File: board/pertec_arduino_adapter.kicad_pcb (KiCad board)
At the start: 2 copper layers, 88.9 x 78.7 mm, 47 parts, among them J1 Conn_02x25_Odd_Even, J2 Conn_02x25_Odd_Even, J3 Conn_02x03_Odd_Even, J4 Conn_01x24, J5 Conn_01x24, J6 Conn_01x05, J7 RJ45_Cetus_J1B1211CCD, J8 Conn_02x03_Odd_Even, Q1 BSS138, Q2 BSS138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

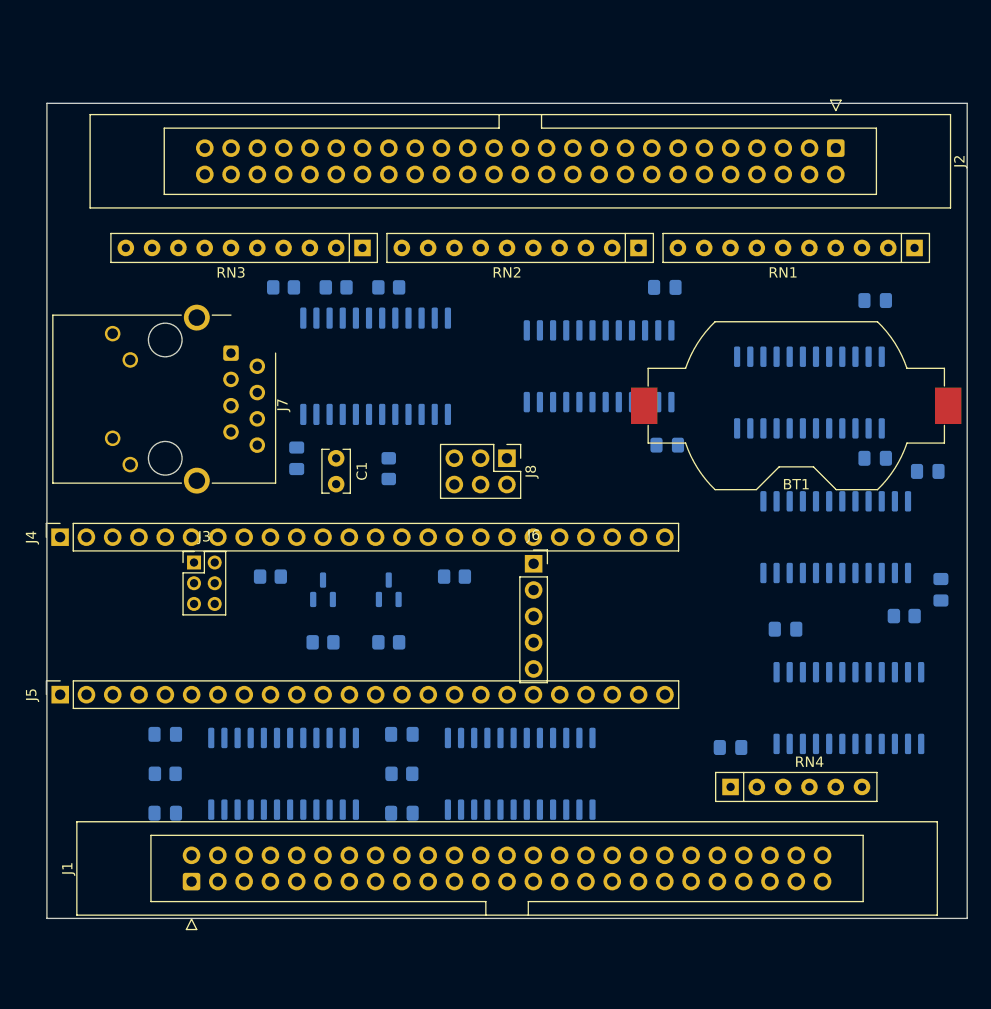
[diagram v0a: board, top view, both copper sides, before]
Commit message: Development checkpoint: added switchable controller/peripheral functionality.
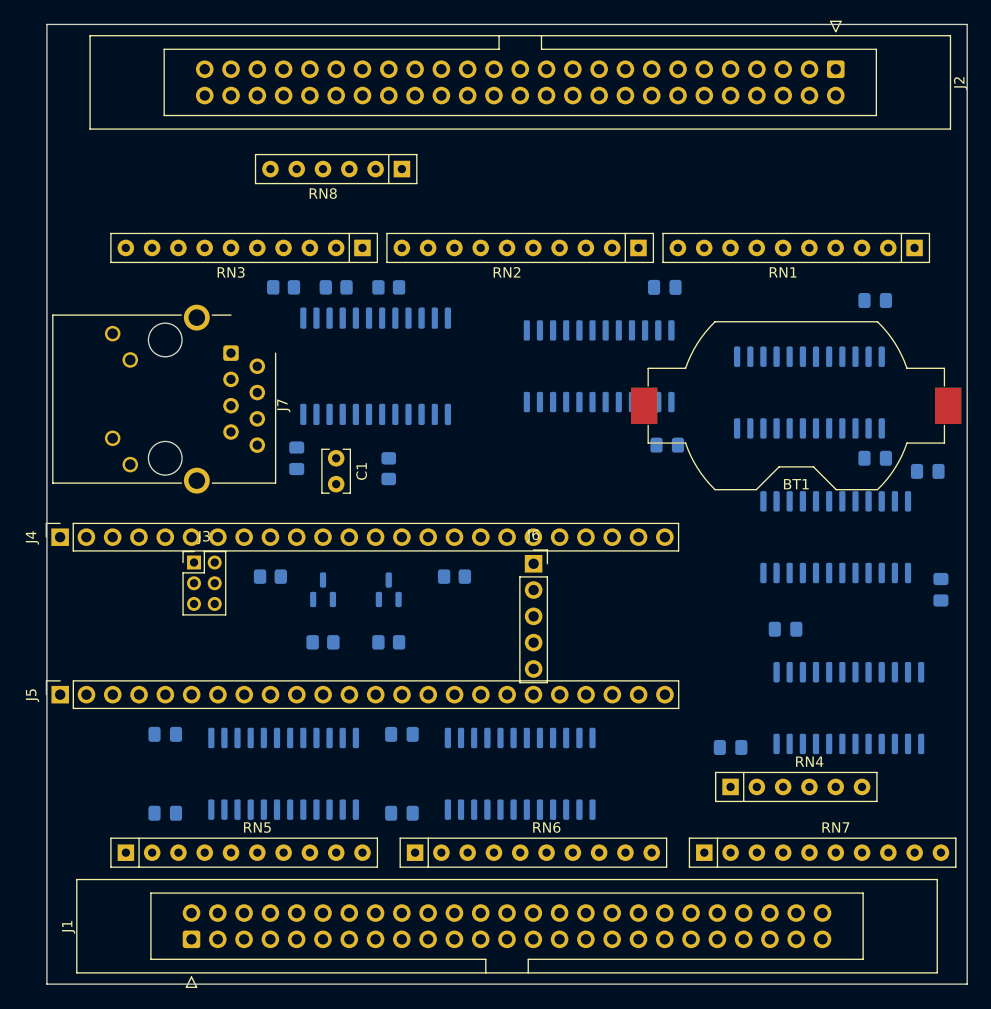
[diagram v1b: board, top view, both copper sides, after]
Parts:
- removed J8: Conn_02x03_Odd_Even, pertec_arduino_adapter:PinHeader_2x03_P2.54mm_Vertical
- removed R10, R11, R9: 10 kΩ, pertec_arduino_adapter:R_0805_2012Metric_Pad1.20x1.40mm_HandSolder
- added RN5: R1=220Ω, R2=330Ω, pertec_arduino_adapter:R_Array_SIP10, F.Cu at (94.0, 118.1)
- added RN6: R1=220Ω, R2=330Ω, pertec_arduino_adapter:R_Array_SIP10, F.Cu at (121.9, 118.1)
- added RN7: R1=220Ω, R2=330Ω, pertec_arduino_adapter:R_Array_SIP10, F.Cu at (149.9, 118.1)
- added RN8: R1=220Ω, R2=330Ω, pertec_arduino_adapter:R_Array_SIP6, F.Cu at (120.7, 52.1)
- moved J2 7.62 mm to (162.6, 42.4)
- moved J1 5.58 mm to (100.3, 126.5)
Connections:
- net GPIO_AD_B0_02 renamed LVIRP
- net GPIO_AD_B0_03 renamed LVIFMK
- net GPIO_AD_B0_12 renamed LPI2C4_SCL
- net GPIO_AD_B0_13 renamed LPI2C4_SDA
- net GPIO_AD_B1_00 renamed LVIR7
- net GPIO_AD_B1_01 renamed LVIR6
- net GPIO_AD_B1_02 renamed LVIR5
- net GPIO_AD_B1_03 renamed LVIR4
- net GPIO_AD_B1_04 renamed LVIR3
- net GPIO_AD_B1_05 renamed LVIR2
- net GPIO_AD_B1_06 renamed LVIR1
- net GPIO_AD_B1_07 renamed LVIR0
- net GPIO_AD_B1_08 renamed LVIW7
- net GPIO_AD_B1_09 renamed LVIW6
- net GPIO_AD_B1_10 renamed LVIW5
- net GPIO_AD_B1_11 renamed LVIW4
- net GPIO_AD_B1_12 renamed LVIW3
- net GPIO_AD_B1_13 renamed LVIW2
- net GPIO_AD_B1_14 renamed LVIW1
- net GPIO_AD_B1_15 renamed LVIW0
- net GPIO_B0_00 renamed LVIWRT
- net GPIO_B0_01 renamed LVIERASE
- net GPIO_B0_02 renamed LVIEDIT
- net GPIO_B0_03 renamed LVILWD
- net GPIO_B0_10 renamed LVIGO
- net GPIO_B0_11 renamed LVIREV
- net GPIO_B0_12 renamed LVIWFM
- net GPIO_B1_00 renamed LVIREW
- net GPIO_B1_01 renamed LVIWP
- net GPIO_B1_02 renamed LVIRSTR
- net GPIO_B1_03 renamed LVIWSTR
- net GPIO_B1_12 renamed LVIHER
- net GPIO_B1_13 renamed LVICER
- net GPIO_EMC_04 renamed LVIRDY
- net GPIO_EMC_06 renamed LVIDBY
- net GPIO_EMC_07 renamed LVIFBY
- net GPIO_EMC_08 renamed ~{LPI2C4_INT}
- net GPIO_EMC_36 renamed LVIEOT
- net GPIO_EMC_37 renamed LVIOFL
- J5 pad 20: GPIO_EMC_32 -> DIRB
- J5 pad 21: GPIO_EMC_31 -> OEA
- J5 pad 5: GPIO_EMC_05 -> DIRA
- U1 pad 18: ILDP -> unconnected-(U1-Pad18)
- U1 pad 2: GNDREF -> DIRA
- U1 pad 22: GNDREF -> OEA
- U1 pad 6: GPIO_EMC_32 -> unconnected-(U1-Pad6)
- U2 pad 2: Net-(U2-Pad2) -> DIRB
- U3 pad 17: IFPT -> unconnected-(U3-Pad17)
- U3 pad 2: GNDREF -> DIRA
- U3 pad 22: GNDREF -> OEA
- U3 pad 7: GPIO_EMC_05 -> unconnected-(U3-Pad7)
- U4 pad 2: Net-(U4-Pad2) -> DIRB
- U5 pad 2: GNDREF -> DIRA
- U5 pad 22: GNDREF -> OEA
- U6 pad 2: Net-(U6-Pad2) -> DIRB
- U7 pad 19: SPARE0 -> ILDP
- U7 pad 20: SPARE1 -> IFPT
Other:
- board size 88.9 x 78.7 mm -> 88.9 x 92.7 mm

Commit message: Development checkpoint: ready to start layout
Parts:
- added JP1: ISGL/SPCMD1, pertec_arduino_adapter:PinHeader_1x02_P2.54mm_Vertical, F.Cu at (113.0, 121.9)
- moved C1 21.1 mm to (102.9, 62.2), turned to 0 degrees
- moved J1 3.81 mm to (100.3, 130.3)
- moved RN1 1.27 mm to (170.2, 58.4)
- moved RN2 1.27 mm to (143.5, 58.4)
- moved RN3 1.27 mm to (116.8, 58.4)
- renumbered U3 to U2, U5 to U3, U6 to U5, U2 to U6
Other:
- board size 88.9 x 92.7 mm -> 88.9 x 96.5 mm

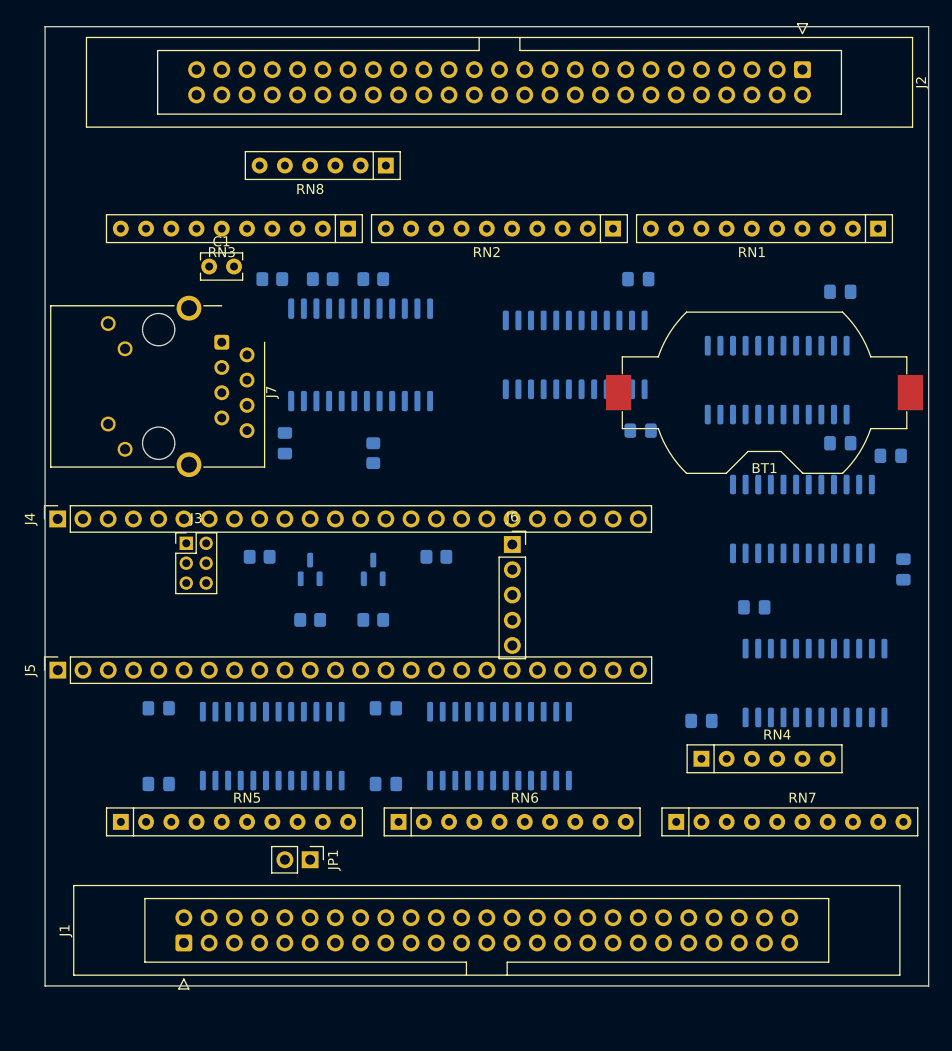
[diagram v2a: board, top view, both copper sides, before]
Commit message: Development checkpoint: fully routed.  Still 6 layers, but I'll chop that down right before tapeout.
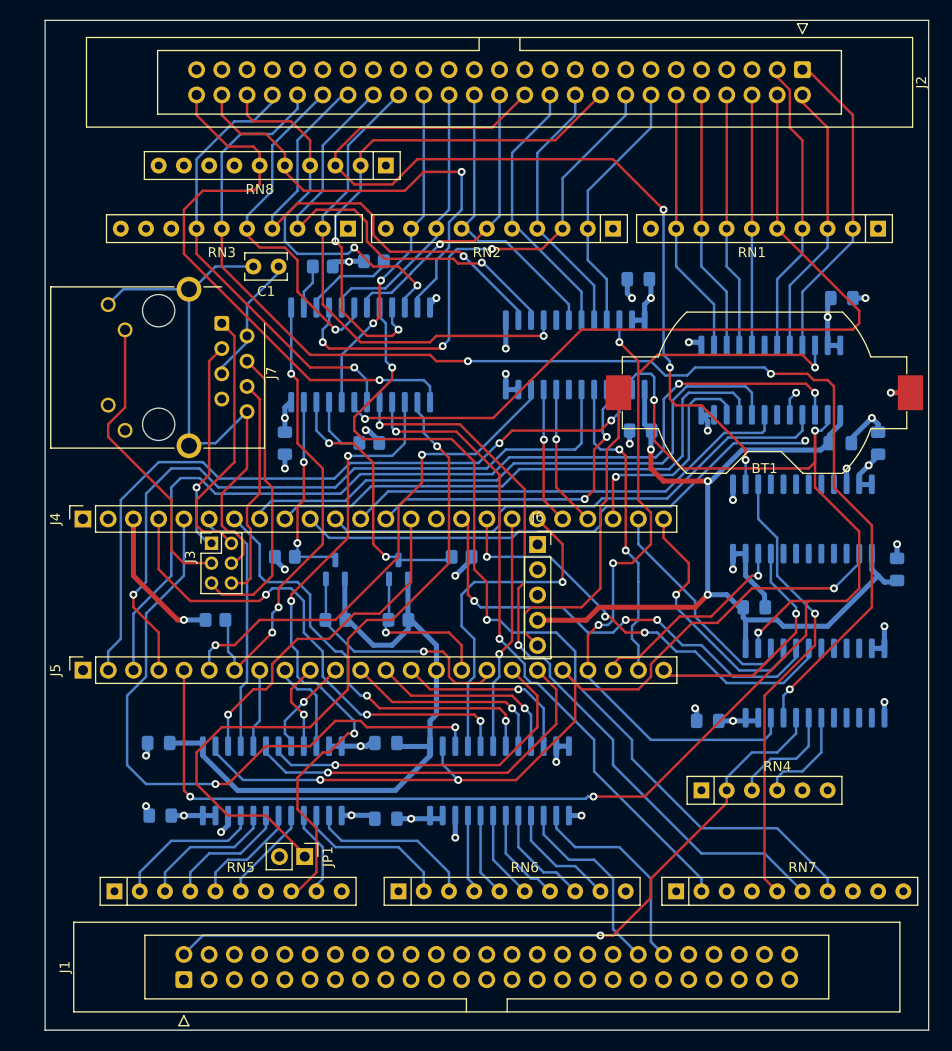
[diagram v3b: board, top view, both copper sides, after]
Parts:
- RN8: footprint pertec_arduino_adapter:R_Array_SIP6 -> pertec_arduino_adapter:R_Array_SIP10
- moved R7 34.8 mm to (103.5, 97.8)
- moved RN5 7.01 mm to (93.3, 125.1)
- moved RN6 6.99 mm to (121.9, 125.1)
- moved RN7 6.99 mm to (149.9, 125.1)
- moved C1 6.98 mm to (109.9, 62.2), turned to 180 degrees
- moved J1 3.69 mm to (100.3, 134.0)
- moved C8 3.49 mm to (120.7, 117.8)
- moved U4 3.49 mm to (132.1, 114.0)
- moved U6 3.49 mm to (109.2, 114.0)
- moved C3 3.49 mm to (97.8, 110.2)
- moved C7 3.49 mm to (120.7, 110.2)
- moved C10 3.18 mm to (97.9, 117.5)
- moved RN4 3.17 mm to (152.4, 114.9)
- moved J3 2.54 mm to (103.1, 90.1)
- moved J4 2.54 mm to (90.2, 87.6)
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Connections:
- J6 pad 4: unconnected-(J6-Pad4) -> +3V3
- RN7 pad 9: IDEN -> unconnected-(RN7-Pad9)
- RN8 pad 6: +5V -> IDEN
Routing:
- net +3V3: track 0.00 -> 168.5 mm, vias 0 -> 4
- net DIRA: track 0.00 -> 149.1 mm, vias 0 -> 5
- net ICER: track 0.00 -> 127.8 mm, vias 0 -> 3
- net ITAD0: track 0.00 -> 105.5 mm, vias 0 -> 2
- net LVIRP: track 0.00 -> 96.0 mm, vias 0 -> 2
- net IOFL: track 0.00 -> 92.2 mm, vias 0 -> 3
- net IRTH1: track 0.00 -> 87.9 mm, vias 0 -> 2
- net DIRB: track 0.00 -> 87.7 mm, vias 0 -> 3
- net OEA: track 0.00 -> 84.8 mm, vias 0 -> 4
- net ISGL: track 0.00 -> 83.7 mm, vias 0 -> 1
- net ILDP: track 0.00 -> 81.9 mm, vias 0 -> 1
- net IRTH2: track 0.00 -> 77.2 mm, vias 0 -> 2
- net ILOL: track 0.00 -> 75.9 mm, vias 0 -> 3
- net IFBY: track 0.00 -> 75.0 mm, vias 0 -> 1
- net LVIFMK: track 0.00 -> 74.5 mm, vias 0 -> 2
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- added copper zone on In1.Cu, net +3V3
- added copper zone on In3.Cu, net +5V
- added copper zone on In2.Cu, net GNDREF
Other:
- board size 88.9 x 96.5 mm -> 88.9 x 101.6 mm
- copper layers 2 -> 6

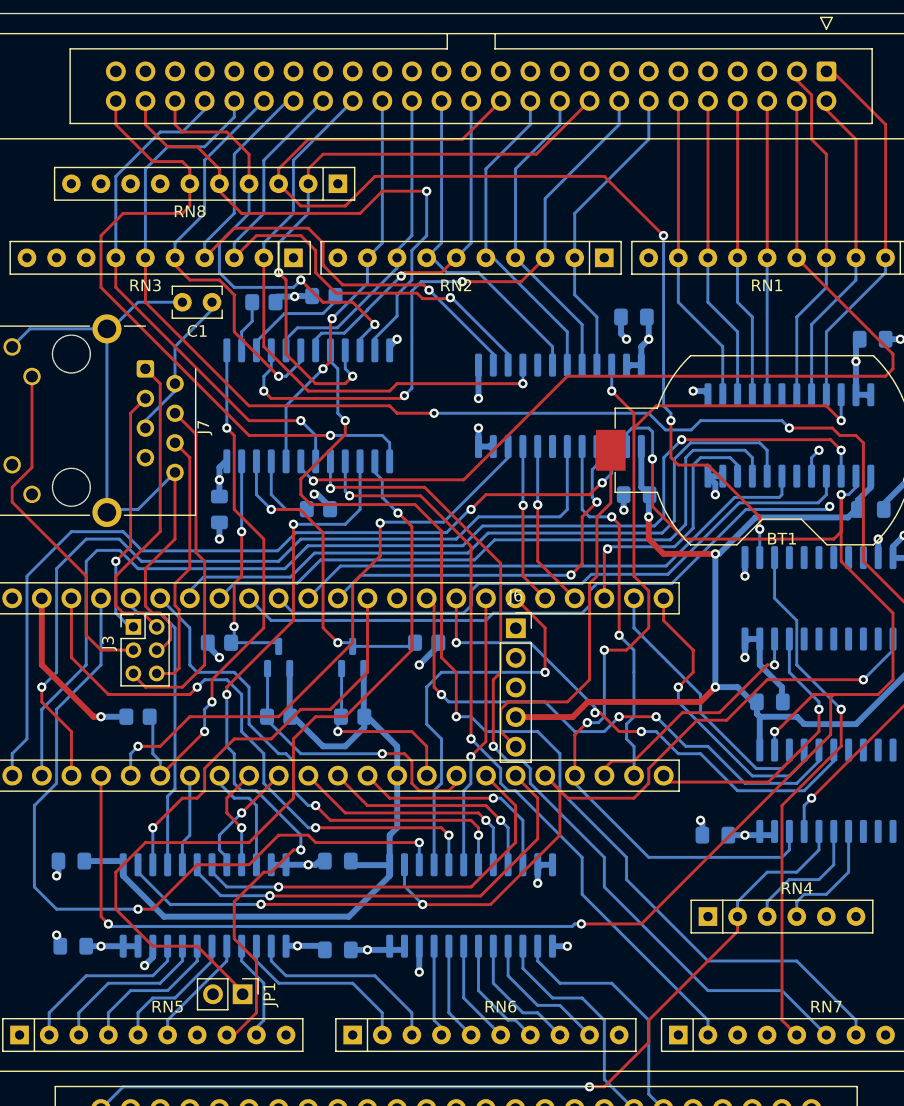
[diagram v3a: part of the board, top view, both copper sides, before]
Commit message: Development checkpoint: layout and routing completed; passes DRC
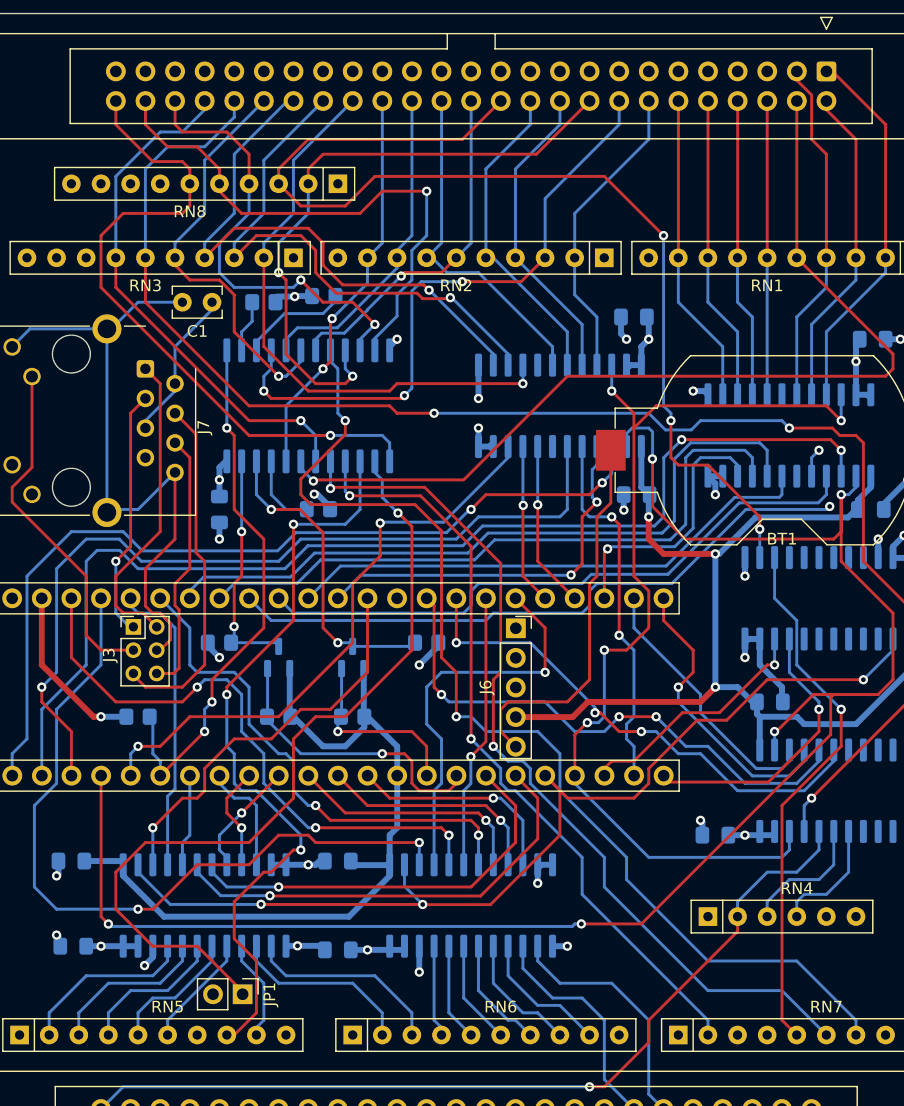
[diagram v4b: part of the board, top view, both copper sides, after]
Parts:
- J1: value Conn_02x25_Odd_Even -> Pertec J1
- J2: value Conn_02x25_Odd_Even -> Pertec J2
- J3: value Conn_02x03_Odd_Even -> Teensy Ethernet; footprint pertec_arduino_adapter:PinSocket_2x03_P2.00mm_Vertical_Mirror -> pertec_arduino_adapter:PinSocket_2x03_P2.00mm_Vertical_Mirror_Teensy4.1_J3
- J4: value Conn_01x24 -> Teensy Right; footprint pertec_arduino_adapter:PinSocket_1x24_P2.54mm_Vertical -> pertec_arduino_adapter:PinSocket_1x24_P2.54mm_Vertical_Teensy4.1_J4
- J5: value Conn_01x24 -> Teensy Left; footprint pertec_arduino_adapter:PinSocket_1x24_P2.54mm_Vertical -> pertec_arduino_adapter:PinSocket_1x24_P2.54mm_Vertical_Teensy4.1_J5
- J6: value Conn_01x05 -> Teensy Cross; footprint pertec_arduino_adapter:PinSocket_1x05_P2.54mm_Vertical -> pertec_arduino_adapter:PinSocket_1x05_P2.54mm_Vertical_Teensy4.1_J6
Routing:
- net LPI2C4_SDA: track 25.8 -> 24.5 mm
- net ISGL: track 83.7 -> 82.6 mm
- net Net-(R5-Pad1): track 9.09 -> 8.22 mm
- net OEA: track 84.8 -> 84.1 mm
- net IEOT: track 27.2 -> 26.6 mm
- net ILOL: track 75.9 -> 75.3 mm
- net Net-(C1-Pad1): track 13.2 -> 12.5 mm
- net LVIW4: track 25.8 -> 25.2 mm
- net LVIW3: track 34.8 -> 34.1 mm
- net LVIW1: track 35.5 -> 34.9 mm
- net LVIW0: track 38.9 -> 38.3 mm
- net LVIOFL: track 21.1 -> 20.5 mm
- net IW7: track 14.8 -> 14.1 mm
- net IRWD: track 27.5 -> 26.9 mm
- net IREV: track 19.0 -> 18.4 mm
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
